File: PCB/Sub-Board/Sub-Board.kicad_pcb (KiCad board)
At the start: 4 copper layers, 50.5 x 113 mm, 200 parts, among them J1 Conn_02x08, J10 Type, J11 Power/I2C, J12 Address, J13 Power/I2C, J14 Address, J15 GPIO, J16 Type, J17 GPIO, J18 Type, J19 Power/I2C, J2 Conn_01x04_Pin, J20 Address, J21 Power/I2C, J22 Address, J23 GPIO, J24 Type, J25 GPIO, J26 Type, J27 Power/I2C, J28 Address, J29 Power/I2C, J3 Power/I2C, J30 Address, J31 GPIO, J32 Type, J33 GPIO, J34 Type, J4 Address, J5 Power/I2C, J6 Address, J7 GPIO, J8 Type, J9 GPIO, SW1 SW_DIP_x07, U1 TPS629210DRLR, U2 74HC165, U3 STM32F401VETx, U4 74HC165, U5 74HC165, U6 74HC165, U7 74HC165, Y1 26 MHz

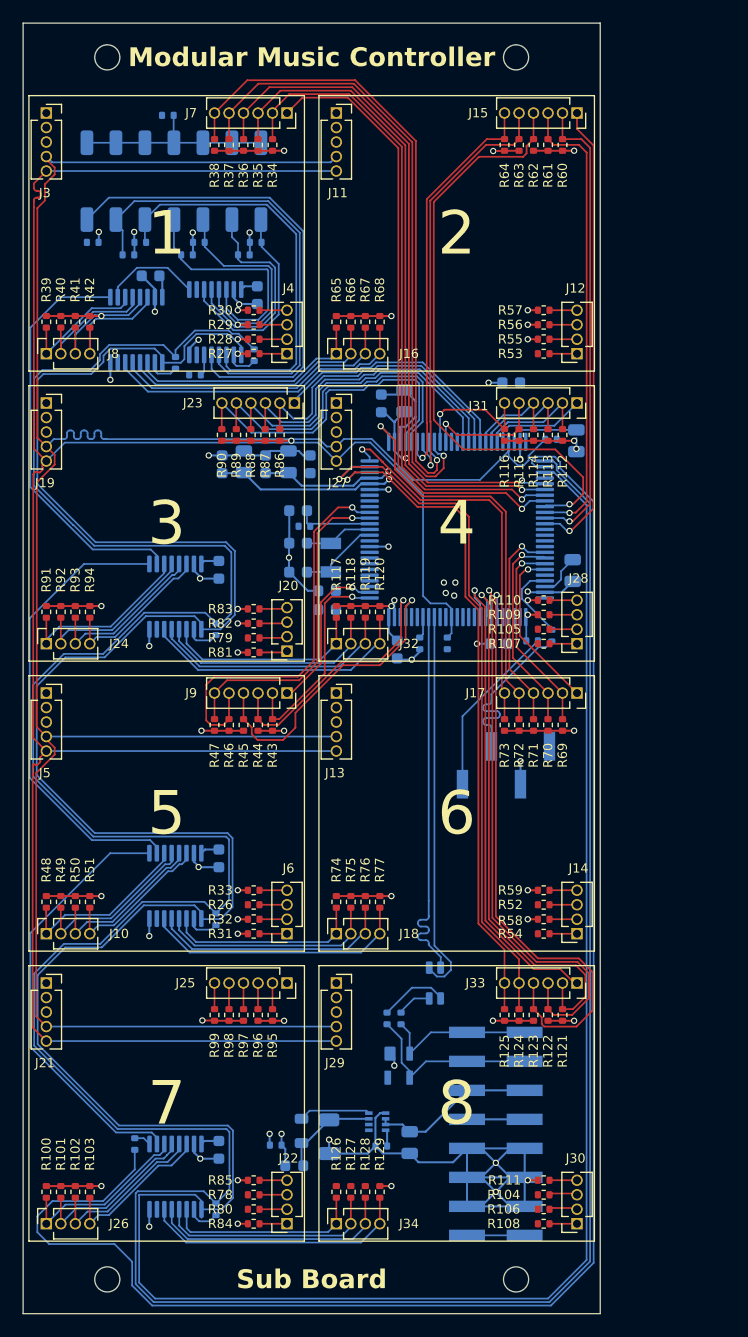
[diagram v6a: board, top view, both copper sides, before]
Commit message: Sub Board: Finished routing with DRC
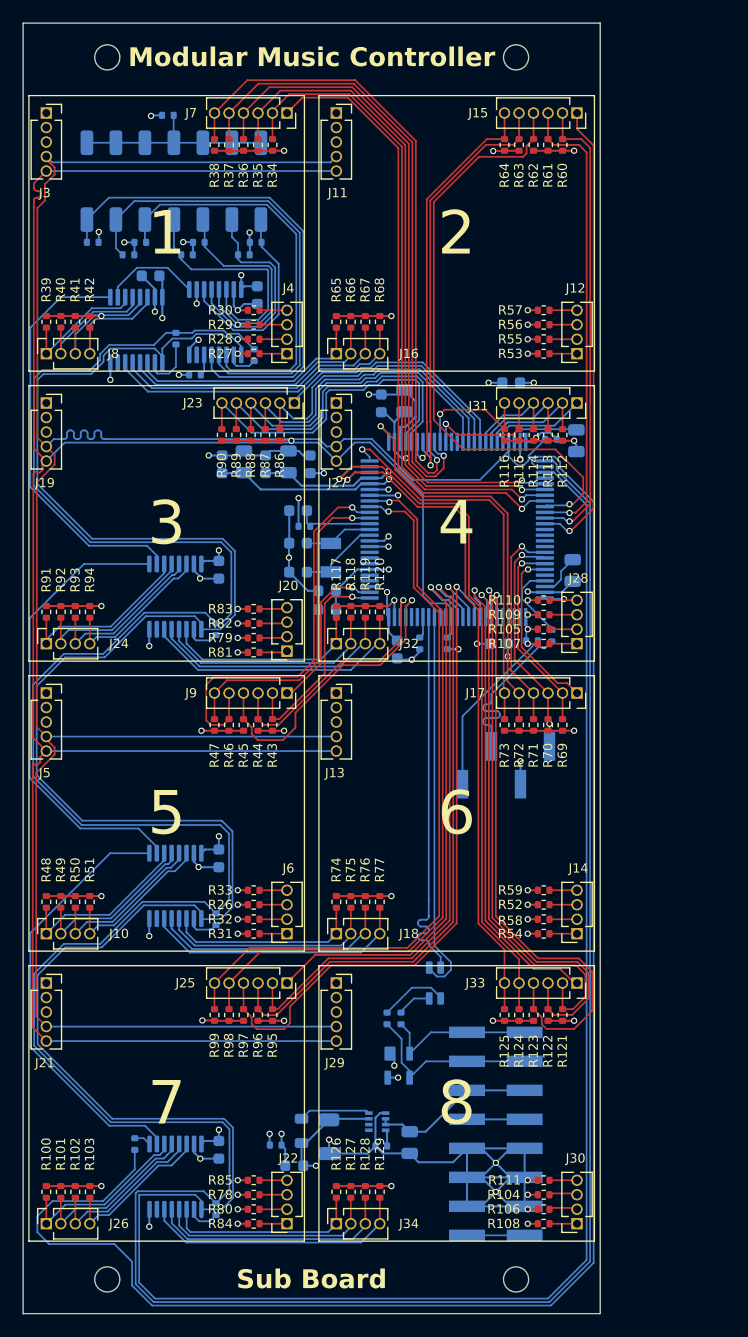
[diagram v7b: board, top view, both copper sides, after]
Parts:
- moved R15 2.12 mm to (115.1, 65.7)
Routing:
- net /STM32-MCU/Slot6.A0: track 2.27 -> 64.3 mm, vias 0 -> 1
- net /STM32-MCU/Slot6.A1: track 2.27 -> 64.1 mm, vias 0 -> 1
- net /STM32-MCU/Slot6.A: track 2.36 -> 59.5 mm
- net /STM32-MCU/Slot6.B: track 2.35 -> 56.0 mm
- net /STM32-MCU/Slot6.C: track 2.27 -> 54.3 mm
- net /STM32-MCU/Slot6.LED: track 0.01 -> 50.4 mm
- net /Board Address/+3.3V Digital: track 27.6 -> 77.0 mm, vias 0 -> 34
- net GND: track 243.1 -> 249.6 mm, vias 71 -> 69
- net /Power Supply/AREF: track 226.1 -> 221.4 mm
- net Net-(U4-CP): track 2.82 -> 4.87 mm
- net /Board Address/BoardAddress6: track 42.8 -> 44.8 mm
- net /STM32-MCU/Config.Clock: track 294.7 -> 293.9 mm
- added copper zone on In1.Cu, net /Board Address/+3.3V Digital
- removed copper zone on In1.Cu, net GND
